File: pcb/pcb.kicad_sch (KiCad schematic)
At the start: 4 parts, among them J1 Botones, J2 Pedales+Velocimetro+Monedas, J3 Volante

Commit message: Add layout and schematic prints
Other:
- title: (none) -> Ches Pur Ofi
- moved on the sheet: A1, J1, J2, J3

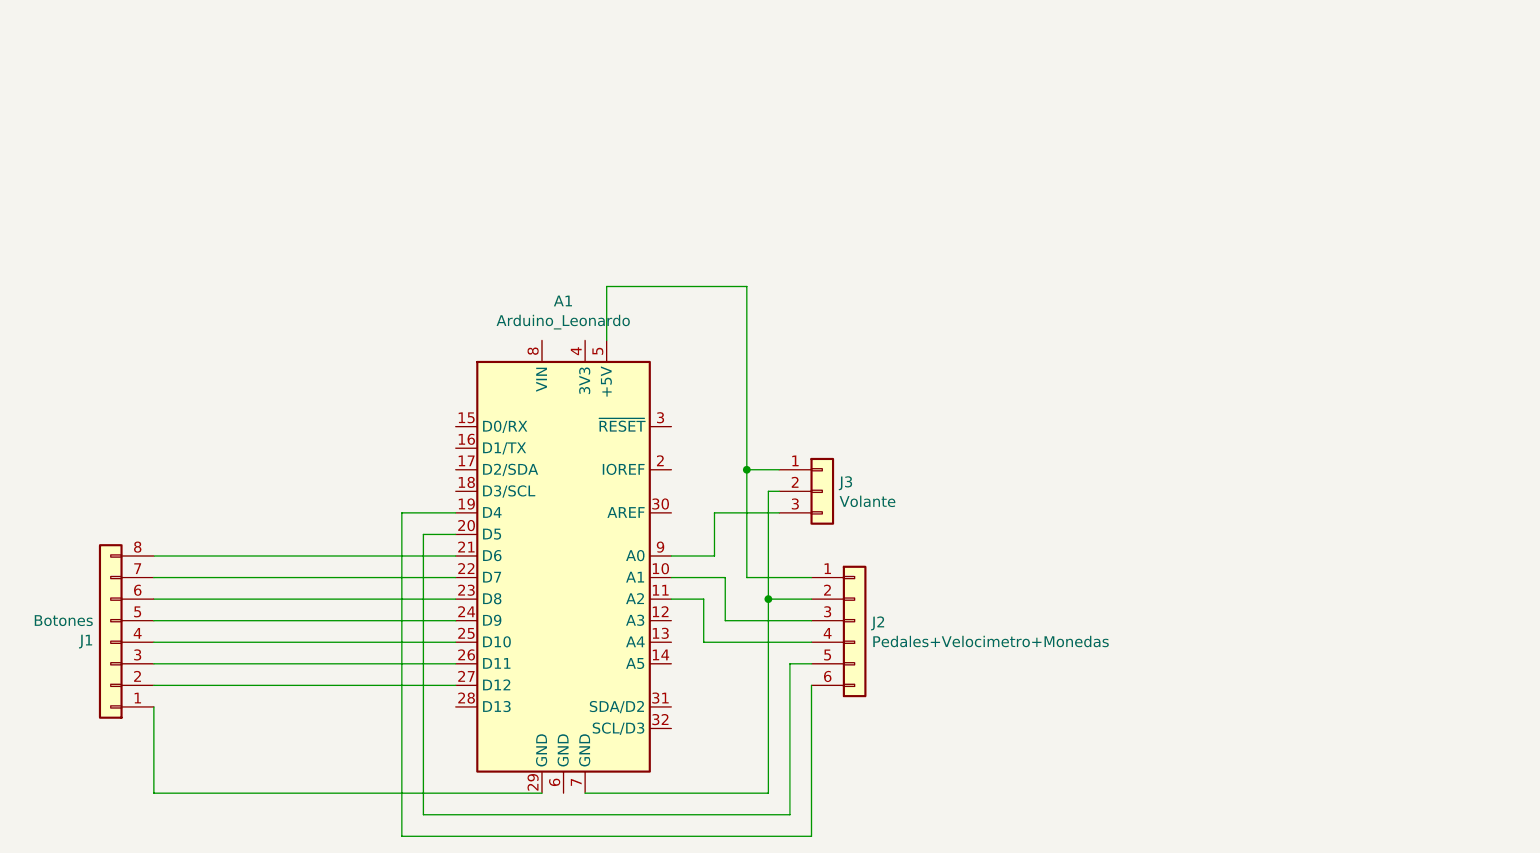
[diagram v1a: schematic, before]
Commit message: Fix schematic wording
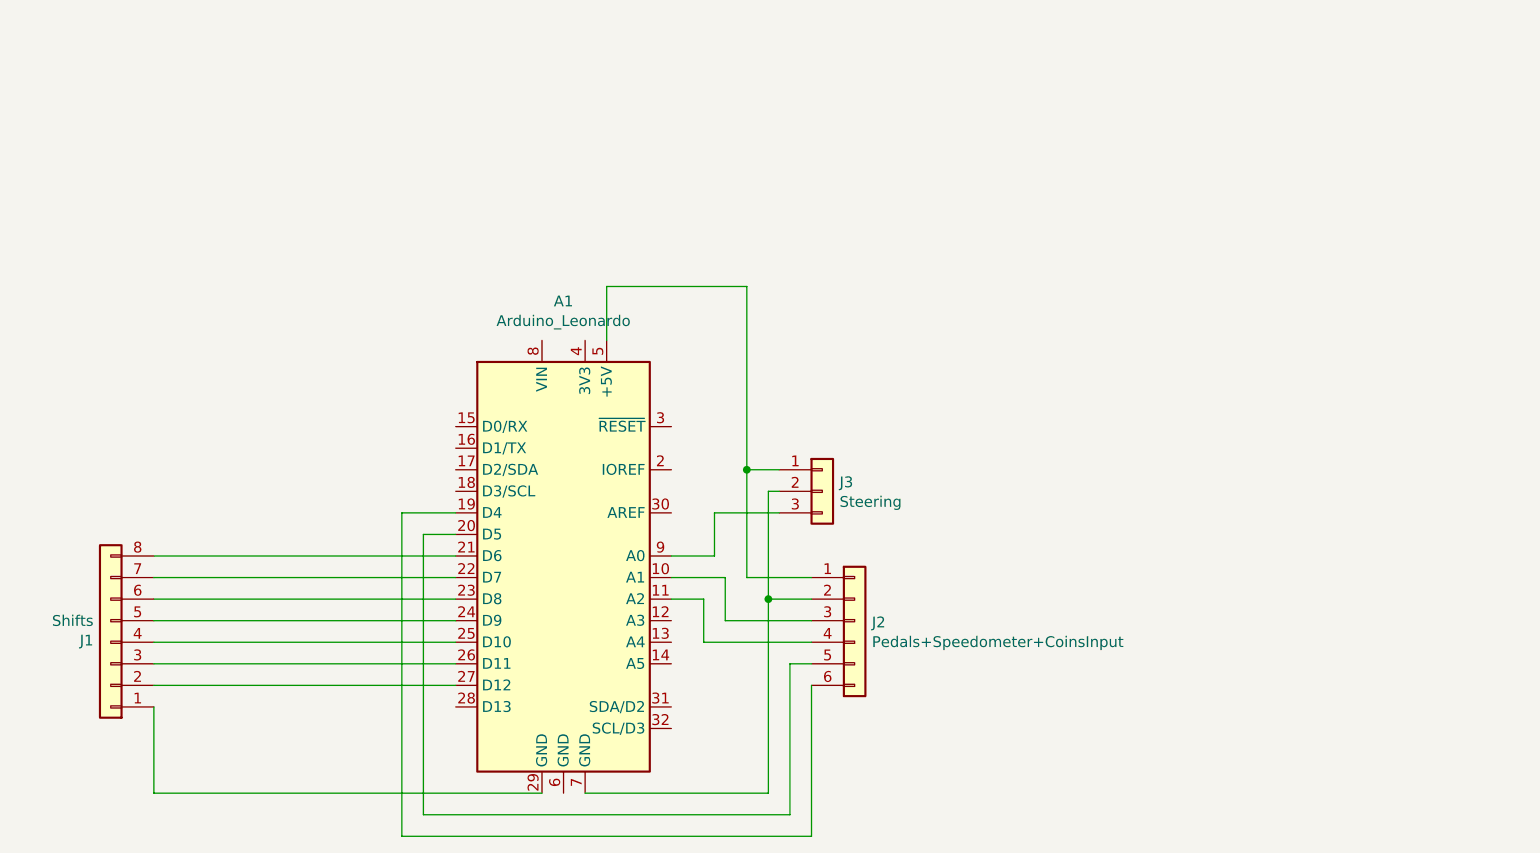
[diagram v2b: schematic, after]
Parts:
- J1: value Botones -> Shifts
- J2: value Pedales+Velocimetro+Monedas -> Pedals+Speedometer+CoinsInput
- J3: value Volante -> Steering
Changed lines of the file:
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@@
       (effects (font (size 1.27 1.27)) (justify left))
     )
-    (property "Value" "Botones" (at 52.578 140.9954 0)
+    (property "Value" "Shifts" (at 52.578 140.9954 0)
       (effects (font (size 1.27 1.27)) (justify left))
     )
@@
       (effects (font (size 1.27 1.27)) (justify left))
     )
-    (property "Value" "Pedales+Velocimetro+Monedas" (at 144.272 143.4846 0)
+    (property "Value" "Pedals+Speedometer+CoinsInput" (at 144.272 143.4846 0)
       (effects (font (size 1.27 1.27)) (justify left))
     )
@@
       (effects (font (size 1.27 1.27)) (justify left))
     )
-    (property "Value" "Volante" (at 140.462 126.9746 0)
+    (property "Value" "Steering" (at 140.462 126.9746 0)
       (effects (font (size 1.27 1.27)) (justify left))
     )

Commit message: Change footprints folder name
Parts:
- A1: footprint custom_footprints:Arduino_Leonardo -> Custom_Footprints:Arduino_Leonardo
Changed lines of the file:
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@@
       (effects (font (size 1.27 1.27)))
     )
-    (property "Footprint" "custom_footprints:Arduino_Leonardo" (at 107.95 133.35 0)
+    (property "Footprint" "Custom_Footprints:Arduino_Leonardo" (at 107.95 133.35 0)
       (effects (font (size 1.27 1.27) italic) hide)
     )
